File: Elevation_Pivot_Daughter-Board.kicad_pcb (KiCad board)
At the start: 4 copper layers, 100 x 176.5 mm, 263 parts, among them CN10 ESW-117-44-L-D, CN11 ESW-108-X-X-D, CN7 ESW-110-44-L-D, CN8 ESW-108-X-X-D, CN9 ESW-115-44-L-D, IC1 TPS1H100BQPWPRQ1, IC2 TPS1H100BQPWPRQ1, J1 1827884, J2 DE9_Socket_MountingHoles, J3 DE9_Socket_MountingHoles, J4 DE9_Socket_MountingHoles, J5 DE9_Socket_MountingHoles, J6 DE9_Socket_MountingHoles, J7 DE9_Socket_MountingHoles, Q1 2N7002KQ-7, Q13 2N7002KQ-7, Q14 IRFS4115TRLPBF, Q15 IRFS4115TRLPBF, Q16 SSM3K361R,LF, Q2 2N7002KQ-7, Q3 2N7002KQ-7, Q4 2N7002KQ-7, Q5 2N7002KQ-7, Q6 2N7002KQ-7, Q7 2N7002KQ-7, U10 ISO6762DWR, U11 TPD2E2U06QDBZRQ1, U12 TPD2E2U06QDBZRQ1, U13 ISO6763DWR, U14 R05CTE05S-R, U15 TCAN1051DRQ1, U16 ISO1432DWR, U17 ESD2CANFD24DBZRQ1, U18 ISO6762DWR, U19 TPD2E2U06QDBZRQ1, U2 ISO6762FQDWRQ1, U20 TPD2E2U06QDBZRQ1, U21 ADS1115BQDGSRQ1, U22 SN74LVC2G07DCKR(UMW), U23 TPS7A2450DBVR, U24 ISO1540DR, U25 TPS7A2450DBVR, U26 TPD1E10B09DPYR, U27 TPD1E10B09DPYR, U3 TPD2E2U06QDBZRQ1, U4 LTC4364IS-2-PBF, U5 TPD2E2U06QDBZRQ1, U6 TPD2E2U06QDBZRQ1, U7 ISO1432DWR, U8 TPD2E2U06QDBZRQ1, U9 TPD2E2U06QDBZRQ1

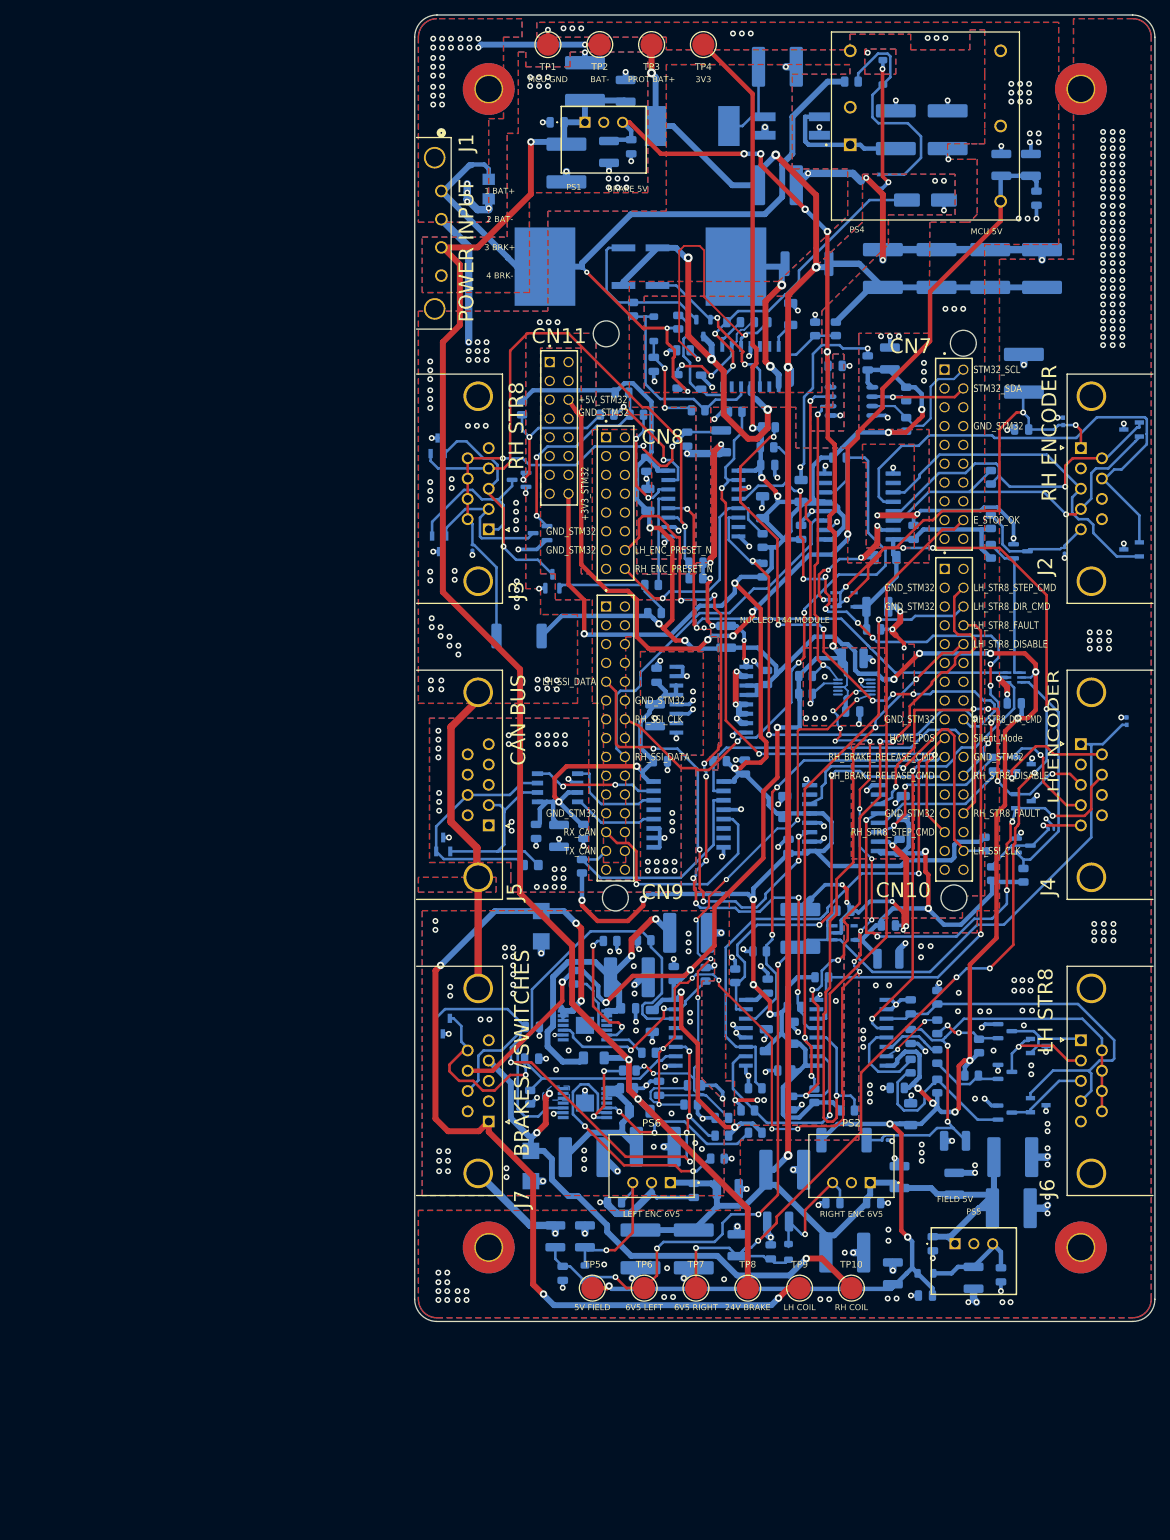
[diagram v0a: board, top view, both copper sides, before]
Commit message: Preserve P5 equal-size placement, controller stack and native BOM
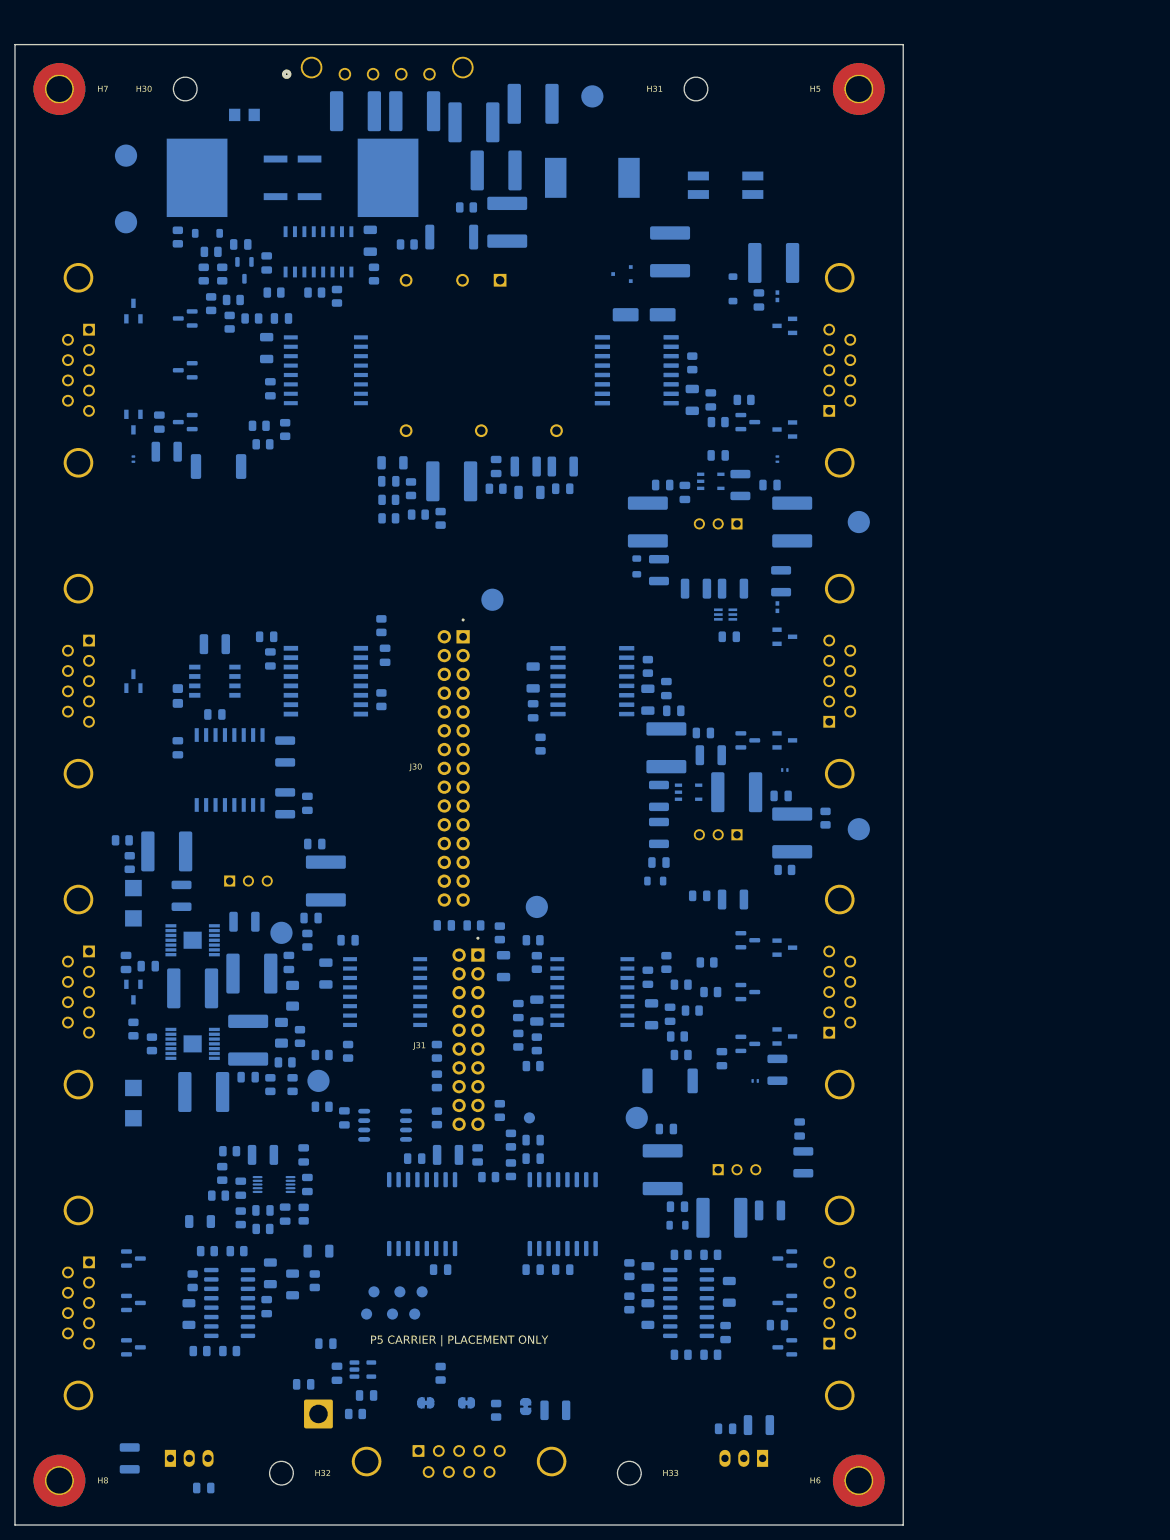
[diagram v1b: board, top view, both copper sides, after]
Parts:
- removed CN10: ESW-117-44-L-D, ESW-117-44-L-D:ESW-117-44-L-D
- removed CN11, CN8: ESW-108-X-X-D, ESW-108-44-L-D:ESW-108-44-L-D
- removed CN7: ESW-110-44-L-D, ESW-110-44-L-D:ESW-110-44-L-D
- removed CN9: ESW-115-44-L-D, ESW-115-44-L-D:ESW-115-44-L-D
- removed H1, H2, H3, H4: MountingHole, MountingHole:MountingHole_3.5mm
- added C110: 10u / 100V, Capacitor_SMD:C_1210_3225Metric, B.Cu at (35.5, 211.0)
- added C111: 10u / 16V, Capacitor_SMD:C_0805_2012Metric, B.Cu at (45.5, 215.0)
- added C112: 1u / 16V, Capacitor_SMD:C_0805_2012Metric, B.Cu at (62.0, 195.5)
- added C113: 1u / 16V, Capacitor_SMD:C_0805_2012Metric, B.Cu at (63.5, 199.5)
- added C114: 1u / 16V, Capacitor_SMD:C_0805_2012Metric, B.Cu at (67.5, 202.5)
- added C115: 100n / 16V, Capacitor_SMD:C_0805_2012Metric, B.Cu at (54.0, 190.5)
- added C116: 100n / 16V, Capacitor_SMD:C_0805_2012Metric, B.Cu at (77.5, 185.5)
- added C117: 100n / 16V, Capacitor_SMD:C_0805_2012Metric, B.Cu at (74.0, 170.5)
- added C140: 10u / 100V, Capacitor_SMD:C_1210_3225Metric, B.Cu at (120.5, 206.5)
- added C141: 10u / 16V, Capacitor_SMD:C_0805_2012Metric, B.Cu at (116.0, 207.0)
- added C142: 1u / 16V, Capacitor_SMD:C_0805_2012Metric, B.Cu at (123.0, 193.0)
- added C145: 100n / 16V, Capacitor_SMD:C_0805_2012Metric, B.Cu at (116.0, 194.0)
- added C160: 100n 16V X7R, Capacitor_SMD:C_0805_2012Metric, B.Cu at (90.0, 170.5)
- added C161: 1u 16V X7R, Capacitor_SMD:C_0805_2012Metric, B.Cu at (90.0, 168.0)
- added C162: 100n 16V X7R, Capacitor_SMD:C_0805_2012Metric, B.Cu at (90.0, 185.5)
- added C163: 1u 16V X7R, Capacitor_SMD:C_0805_2012Metric, B.Cu at (94.0, 185.5)
- added C188: 1n / 1kV, Capacitor_SMD:C_0805_2012Metric, B.Cu at (59.0, 201.0)
- added C190: 100n, Capacitor_SMD:C_0805_2012Metric, B.Cu at (53.5, 177.5)
- added C191: 100n, Capacitor_SMD:C_0805_2012Metric, B.Cu at (50.5, 174.5)
- added H30: M3 STACK SUPPORT, MountingHole:MountingHole_3.2mm_M3, F.Cu at (43.0, 26.0)
- added H31: M3 STACK SUPPORT, MountingHole:MountingHole_3.2mm_M3, F.Cu at (112.0, 26.0)
- added H32: M3 STACK SUPPORT, MountingHole:MountingHole_3.2mm_M3, F.Cu at (56.0, 213.0)
- added H33: M3 STACK SUPPORT, MountingHole:MountingHole_3.2mm_M3, F.Cu at (103.0, 213.0)
- added J12: CHASSIS / SHIELD, Connector_Wire:SolderWire-2sqmm_1x01_D2mm_OD3.9mm, B.Cu at (61.0, 205.0)
- added J20: DE9 FEMALE, Connector_Dsub:DSUB-9_Socket_Horizontal_P2.77x2.84mm_EdgePinOffset7.70mm_Housed_MountingHolesOffset9.12mm, B.Cu at (30.0, 184.5)
- added J21: DE9 FEMALE, Connector_Dsub:DSUB-9_Socket_Horizontal_P2.77x2.84mm_EdgePinOffset7.70mm_Housed_MountingHolesOffset9.12mm, B.Cu at (130.0, 195.5)
- added J22: DE9 MODBUS RTU, Connector_Dsub:DSUB-9_Socket_Horizontal_P2.77x2.84mm_EdgePinOffset7.70mm_Housed_MountingHolesOffset9.12mm, B.Cu at (74.5, 210.0)
- added J30: SSW-115-01-S-D, Stack:Samtec_SSW-115-01-S-D, F.Cu at (78.0, 100.0)
- added J31: SSW-110-01-S-D, Stack:Samtec_SSW-110-01-S-D, F.Cu at (80.0, 143.0)
- added JP160: BIAS, Jumper:SolderJumper-2_P1.3mm_Bridged_RoundedPad1.0x1.5mm, B.Cu at (75.5, 203.5)
- added JP161: BIAS, Jumper:SolderJumper-2_P1.3mm_Bridged_RoundedPad1.0x1.5mm, B.Cu at (81.0, 203.5)
- added JP162: TERM, Jumper:SolderJumper-2_P1.3mm_Bridged_RoundedPad1.0x1.5mm, B.Cu at (89.0, 204.0)
- added PS10: R-78HB5.0-0.5, Converter_DCDC:Converter_DCDC_RECOM_R-78HB-0.5_THT, B.Cu at (41.0, 211.0)
- added PS11: R-78HB5.0-0.5, Converter_DCDC:Converter_DCDC_RECOM_R-78HB-0.5_THT, B.Cu at (121.0, 211.0)
- added R100: 120R 1% / 0.5W, Resistor_SMD:R_1206_3216Metric, B.Cu at (54.5, 186.0)
- added R101: 560R 1%, Resistor_SMD:R_0805_2012Metric, B.Cu at (50.0, 183.0)
- added R102: 560R 1%, Resistor_SMD:R_0805_2012Metric, B.Cu at (46.0, 183.0)
- added R103: 120R 1% / 0.5W, Resistor_SMD:R_1206_3216Metric, B.Cu at (57.5, 187.5)
- added R104: 560R 1%, Resistor_SMD:R_0805_2012Metric, B.Cu at (60.5, 187.0)
- added R105: 560R 1%, Resistor_SMD:R_0805_2012Metric, B.Cu at (49.0, 196.5)
- added R106: 120R 1% / 0.5W, Resistor_SMD:R_1206_3216Metric, B.Cu at (43.5, 191.5)
- added R107: 560R 1%, Resistor_SMD:R_0805_2012Metric, B.Cu at (44.0, 187.0)
- added R108: 560R 1%, Resistor_SMD:R_0805_2012Metric, B.Cu at (45.0, 196.5)
- added R130: 120R 1% / 0.5W, Resistor_SMD:R_1206_3216Metric, B.Cu at (105.5, 191.5)
- added R131: 560R 1%, Resistor_SMD:R_0805_2012Metric, B.Cu at (110.0, 197.0)
- added R132: 560R 1%, Resistor_SMD:R_0805_2012Metric, B.Cu at (114.0, 197.0)
- added R133: 120R 1% / 0.5W, Resistor_SMD:R_1206_3216Metric, B.Cu at (105.5, 186.5)
- added R134: 560R 1%, Resistor_SMD:R_0805_2012Metric, B.Cu at (110.0, 183.5)
- added R135: 560R 1%, Resistor_SMD:R_0805_2012Metric, B.Cu at (114.0, 183.5)
- added R136: 120R 1% / 0.5W, Resistor_SMD:R_1206_3216Metric, B.Cu at (116.5, 188.5)
- added R137: 560R 1%, Resistor_SMD:R_0805_2012Metric, B.Cu at (103.0, 190.0)
- added R138: 560R 1%, Resistor_SMD:R_0805_2012Metric, B.Cu at (103.0, 185.5)
- added R160: 10k, Resistor_SMD:R_0805_2012Metric, B.Cu at (87.0, 172.0)
- added R161: 10k, Resistor_SMD:R_0805_2012Metric, B.Cu at (87.0, 168.0)
- added R162: 10k, Resistor_SMD:R_0805_2012Metric, B.Cu at (84.0, 173.0)
- added R163: 560R 1%, Resistor_SMD:R_0805_2012Metric, B.Cu at (77.5, 199.5)
- added R164: 560R 1%, Resistor_SMD:R_0805_2012Metric, B.Cu at (85.0, 204.5)
- added R165: 120R 1% 0.5W, Resistor_SMD:R_1210_3225Metric, B.Cu at (93.0, 204.5)
- added R172: 0R - BOND OPTION, Resistor_SMD:R_0805_2012Metric, B.Cu at (66.0, 205.0)
- added R180: 10k 0.1%, Resistor_SMD:R_0805_2012Metric, B.Cu at (47.5, 175.5)
- added R181: 10k 0.1%, Resistor_SMD:R_0805_2012Metric, B.Cu at (59.0, 178.0)
- added R182: 1k, Resistor_SMD:R_0805_2012Metric, B.Cu at (50.5, 178.5)
- added R183: 1k, Resistor_SMD:R_0805_2012Metric, B.Cu at (53.5, 180.0)
- added TH1: 10k NTC / 1206, Resistor_SMD:R_1206_3216Metric, B.Cu at (45.0, 179.0)
- added TH2: 10k NTC / 1206, Resistor_SMD:R_1206_3216Metric, B.Cu at (61.0, 183.0)
- added TP20: TP20, TestPoint:TestPoint_Pad_D1.5mm, B.Cu at (68.5, 188.5)
- added TP21: TP21, TestPoint:TestPoint_Pad_D1.5mm, B.Cu at (72.0, 188.5)
- added TP22: TP22, TestPoint:TestPoint_Pad_D1.5mm, B.Cu at (75.0, 188.5)
- added TP23: TP23, TestPoint:TestPoint_Pad_D1.5mm, B.Cu at (67.5, 191.5)
- added TP24: TP24, TestPoint:TestPoint_Pad_D1.5mm, B.Cu at (71.0, 191.5)
- added TP25: TP25, TestPoint:TestPoint_Pad_D1.5mm, B.Cu at (74.0, 191.5)
- added TP30: CTRL_NRST, TestPoint:TestPoint_Pad_D1.5mm, B.Cu at (89.5, 165.0)
- added U100: AM26LV32EIDR, Package_SO:SOIC-16_3.9x9.9mm_P1.27mm, B.Cu at (49.0, 190.0)
- added U101: ISO7760FDWR, Package_SO:SOIC-16W_7.5x10.3mm_P1.27mm, B.Cu at (75.0, 178.0)
- added U102: TPD2E2U06QDBZRQ1, Package_TO_SOT_SMD:SOT-23, B.Cu at (36.0, 184.0)
- added U103: TPD2E2U06QDBZRQ1, Package_TO_SOT_SMD:SOT-23, B.Cu at (36.0, 190.0)
- added U104: TPD2E2U06QDBZRQ1, Package_TO_SOT_SMD:SOT-23, B.Cu at (36.0, 196.0)
- added U105: TLV75533PDBVR, Package_TO_SOT_SMD:SOT-23-5, B.Cu at (67.0, 199.0)
- added U110: AM26LV32EIDR, Package_SO:SOIC-16_3.9x9.9mm_P1.27mm, B.Cu at (111.0, 190.0)
- added U112: TPD2E2U06QDBZRQ1, Package_TO_SOT_SMD:SOT-23, B.Cu at (124.0, 184.0)
- added U113: TPD2E2U06QDBZRQ1, Package_TO_SOT_SMD:SOT-23, B.Cu at (124.0, 190.0)
- added U114: TPD2E2U06QDBZRQ1, Package_TO_SOT_SMD:SOT-23, B.Cu at (124.0, 196.0)
- added U160: ISO1410DWR, Package_SO:SOIC-16W_7.5x10.3mm_P1.27mm, B.Cu at (94.0, 178.0)
- J1, J2, J3, J4, J5, J6, J7, PS1, PS2, PS4, PS5, PS6, TP1, TP2, TP3, TP4, TP5, TP8: moved to B.Cu
- TP10: value RH_BRAKE_COIL -> STAR_BRAKE_COIL; moved to B.Cu
- TP6: value +6.5V_ENC_L -> +6.5V_ENC_PORT; moved to B.Cu
- TP7: value +6.5V_ENC_R -> +6.5V_ENC_STAR; moved to B.Cu
- TP9: value LH_BRAKE_COIL -> PORT_BRAKE_COIL; moved to B.Cu
- moved TP8 174.5 mm to (35.0, 35.0)
- moved C7 124.2 mm to (42.5, 135.0)
- moved C87 123.1 mm to (78.5, 170.0), turned to 0 degrees
- moved C90 121.3 mm to (64.5, 165.0), turned to 90 degrees
- moved C88 119.3 mm to (82.5, 170.0), turned to 90 degrees
- moved TP4 118.7 mm to (90.5, 136.5)
- moved R67 116.6 mm to (77.0, 165.0)
- moved U24 116.3 mm to (70.0, 166.0)
- moved C23 115.1 mm to (51.0, 138.5), turned to 180 degrees
- moved C21 113.5 mm to (62.0, 133.0)
- moved PS1 113.2 mm to (49.0, 133.0)
- moved C1 112.8 mm to (60.0, 138.0), turned to 0 degrees
- moved R68 107.7 mm to (85.5, 164.0), turned to 90 degrees
- moved C11 107.5 mm to (40.5, 129.0), turned to 0 degrees
- moved TP7 105.8 mm to (134.0, 84.5)
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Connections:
- net +5V_ENC_L renamed +5V_ENC_PORT
- net +5V_ENC_R renamed +5V_ENC_STAR
- net +6.5V_ENC_L renamed +6.5V_ENC_PORT
- net +6.5V_ENC_R renamed +6.5V_ENC_STAR
- net /ADS1115/LH_BRAKE_CURR renamed /ADS1115/PORT_BRAKE_CURR
- net /ADS1115/RH_BRAKE_CURR renamed /ADS1115/STAR_BRAKE_CURR
- net /Brakes/LH_BRAKE_RELEASE_CMD renamed /Brakes/PORT_BRAKE_RELEASE_CMD
- net /Brakes/RH_BRAKE_RELEASE_CMD renamed /Brakes/STAR_BRAKE_RELEASE_CMD
- net /SSI_Encoder/LH_SSI_CLK renamed /Controller_Interface/PORT_SSI_CLK
- net /SSI_Encoder/RH_SSI_CLK renamed /Controller_Interface/STAR_SSI_CLK
- net /STM32/LH_ENC_PRESET_N renamed /Controller_Interface/PORT_ENC_PRESET_N
- net /STM32/LH_STR8_DIR_CMD renamed /Controller_Interface/PORT_STR8_DIR_CMD
- net /STM32/LH_STR8_DISABLE renamed /Controller_Interface/PORT_STR8_DISABLE
- net /STM32/LH_STR8_FAULT renamed /Controller_Interface/PORT_STR8_FAULT
- net /STM32/LH_STR8_STEP_CMD renamed /Controller_Interface/PORT_STR8_STEP_CMD
- net /STM32/RH_ENC_PRESET_N renamed /Controller_Interface/STAR_ENC_PRESET_N
- net /STM32/RH_STR8_DIR_CMD renamed /Controller_Interface/STAR_STR8_DIR_CMD
- net /STM32/RH_STR8_DISABLE renamed /Controller_Interface/STAR_STR8_DISABLE
- net /STM32/RH_STR8_FAULT renamed /Controller_Interface/STAR_STR8_FAULT
- net /STM32/RH_STR8_STEP_CMD renamed /Controller_Interface/STAR_STR8_STEP_CMD
- net /STM32/Silent_Mode renamed /Controller_Interface/Silent_Mode
- net /STM32/TX_CAN renamed /Controller_Interface/TX_CAN
- net LH_BRAKE_COIL renamed PORT_BRAKE_COIL
- net LH_ENC_CLK_N renamed PORT_ENC_CLK_N
- net LH_ENC_CLK_P renamed PORT_ENC_CLK_P
- net LH_ENC_DATA_N renamed PORT_ENC_DATA_N
- net LH_ENC_DATA_P renamed PORT_ENC_DATA_P
- net LH_ENC_POS_PRESET renamed PORT_ENC_POS_PRESET
- net LH_STR8_5V_FIELD renamed PORT_STR8_5V_FIELD
- net LH_STR8_FAULT_RAW renamed PORT_STR8_FAULT_RAW
- net RH_BRAKE_COIL renamed STAR_BRAKE_COIL
- net RH_ENC_CLK_N renamed STAR_ENC_CLK_N
- net RH_ENC_CLK_P renamed STAR_ENC_CLK_P
- net RH_ENC_DATA_N renamed STAR_ENC_DATA_N
- net RH_ENC_DATA_P renamed STAR_ENC_DATA_P
- net RH_ENC_POS_PRESET renamed STAR_ENC_POS_PRESET
- net RH_STR8_5V_FIELD renamed STAR_STR8_5V_FIELD
- net RH_STR8_FAULT_RAW renamed STAR_STR8_FAULT_RAW
- U13 pad 5: /STM32/RX_CAN -> /Controller_Interface/RX_CAN
- U16 pad 3: /SSI_Encoder/RH_SSI_DATA -> /Controller_Interface/STAR_SSI_DATA
- U21 pad 6: unconnected-(U21-AIN2-Pad6) -> /ADS1115/TEMP_BOARD
- U21 pad 7: unconnected-(U21-AIN3-Pad7) -> /ADS1115/TEMP_POWER
- U7 pad 3: /SSI_Encoder/LH_SSI_DATA -> /Controller_Interface/PORT_SSI_DATA
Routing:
- net -BATT: track 409.0 -> 0.00 mm, vias 343 -> 0
- net +3V3_STM32: track 391.6 -> 0.00 mm, vias 13 -> 0
- net +5V_FIELD: track 334.6 -> 0.00 mm, vias 15 -> 0
- net +BATT_Prot: track 319.0 -> 0.00 mm, vias 5 -> 0
- net +5V_BRAKE: track 249.4 -> 0.00 mm, vias 12 -> 0
- net +6.5V_ENC_STAR: track 223.9 -> 0.00 mm, vias 12 -> 0
- net +24V_BRAKE: track 206.6 -> 0.00 mm, vias 3 -> 0
- net +6.5V_ENC_PORT: track 151.4 -> 0.00 mm, vias 4 -> 0
- net /ADS1115/PORT_BRAKE_CURR: track 139.9 -> 0.00 mm, vias 17 -> 0
- net +5V_STM32: track 137.0 -> 0.00 mm, vias 4 -> 0
- net PORT_BRAKE_COIL: track 131.2 -> 0.00 mm, vias 5 -> 0
- net +BATT: track 112.5 -> 0.00 mm, vias 3 -> 0
- net /Brakes/E_STOP_OK: track 109.8 -> 0.00 mm, vias 1 -> 0
- net /Controller_Interface/PORT_ENC_PRESET_N: track 103.4 -> 0.00 mm, vias 9 -> 0
- net /Controller_Interface/PORT_STR8_STEP_CMD: track 98.2 -> 0.00 mm, vias 5 -> 0
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- removed copper zone on B.Cu, net -BATT
- removed copper zone on F.Cu, net -BATT
- removed copper zone on In1.Cu, net -BATT
- removed copper zone on In2.Cu, net -BATT
- removed copper zone on B.Cu, net GND_BRAKE
- removed copper zone on F.Cu, net GND_BRAKE
- removed copper zone on In1.Cu, net GND_BRAKE
- removed copper zone on In2.Cu, net GND_BRAKE
- removed copper zone on B.Cu, net GND_CAN
- removed copper zone on F.Cu, net GND_CAN
- removed copper zone on In1.Cu, net GND_CAN
- removed copper zone on In2.Cu, net GND_CAN
- removed copper zone on B.Cu, net GND_FLOAT
- removed copper zone on F.Cu, net GND_FLOAT
- removed copper zone on In1.Cu, net GND_FLOAT
- removed copper zone on In2.Cu, net GND_FLOAT
- removed copper zone on B.Cu, net GND_STM32
- removed copper zone on F.Cu, net GND_STM32
- removed copper zone on In1.Cu, net GND_STM32
- removed copper zone on In2.Cu, net GND_STM32
- removed copper zone on In1.Cu, net Net-(PS4--VIN)
- removed copper zone on In2.Cu, net Net-(PS4--VIN)
- removed copper zone on B.Cu, net STAR_BRAKE_COIL
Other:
- board size 100 x 176.5 mm -> 120 x 200 mm
- board text added: "120 x 200 mm / 4 layers / NO ROUTING"
- board text added: "BRAKES"
- board text added: "CAN"
- board text added: "MODBUS"
- board text added: "OUTWARD FACE: BOTTOM"
- board text added: "P5 CARRIER | PLACEMENT ONLY"
- board text added: "PORT MOTOR"
- board text added: "PORT SSI"
- board text added: "PORT STEP"
- board text added: "POWER IN"
- board text added: "STAR MOTOR"
- board text added: "STAR SSI"
- board text added: "STAR STEP"
- board text removed: "*"
- board text removed: "+3V3_STM32"
- board text removed: "+5V_STM32"
- board text removed: "1 BAT+"
- board text removed: "2 BAT-"
- board text removed: "24V BRAKE"
- board text removed: "3 BRK+"
- board text removed: "3V3"
- board text removed: "4 BRK-"
- board text removed: "5V FIELD"
- board text removed: "6V5 LEFT"
- board text removed: "6V5 RIGHT"
- board text removed: "BAT-"
- board text removed: "BRAKE 5V"
- board text removed: "BRAKES / SWITCHES"
- board text removed: "CAN BUS"
- board text removed: "E_STOP_OK"
- board text removed: "FIELD 5V"
- board text removed: "GND_STM32"
- board text removed: "HOME_POS"
- board text removed: "LEFT ENC 6V5"
- board text removed: "LH COIL"
- board text removed: "LH COIL POWER"
- board text removed: "LH ENCODER"
- board text removed: "LH STR8"
- board text removed: "LH_BRAKE_RELEASE_CMD"
- board text removed: "LH_ENC_PRESET_N"
- board text removed: "LH_SSI_CLK"
- board text removed: "LH_SSI_DATA"
- board text removed: "LH_STR8_DIR_CMD"
- board text removed: "LH_STR8_DISABLE"
- board text removed: "LH_STR8_FAULT"
- board text removed: "LH_STR8_STEP_CMD"
- board text removed: "MCU 5V"
- board text removed: "MCU GND"
- board text removed: "NUCLEO-144 MODULE"
- board text removed: "POWER INPUT"
- board text removed: "PROT BAT+"
- board text removed: "RH COIL"
- board text removed: "RH COIL POWER"
- board text removed: "RH ENCODER"
- board text removed: "RH STR8"
- board text removed: "RH_BRAKE_RELEASE_CMD"
- board text removed: "RH_ENC_PRESET_N"
- board text removed: "RH_SSI_CLK"
- board text removed: "RH_SSI_DATA"
- board text removed: "RH_STR8_DIR_CMD"
- board text removed: "RH_STR8_DISABLE"
- board text removed: "RH_STR8_FAULT"
- board text removed: "RH_STR8_STEP_CMD"
- board text removed: "RIGHT ENC 6V5"
- board text removed: "RX_CAN"
- board text removed: "STM32_SCL"
- board text removed: "STM32_SDA"
- board text removed: "Silent_Mode"
- board text removed: "TX_CAN"
